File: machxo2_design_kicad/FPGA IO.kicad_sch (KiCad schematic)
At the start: 7 parts, among them J2 Conn_01x12_Pin, J3 Conn_01x12_Pin, Q3 DMG1012T, U3 LCMX02-256HC-4SG32C

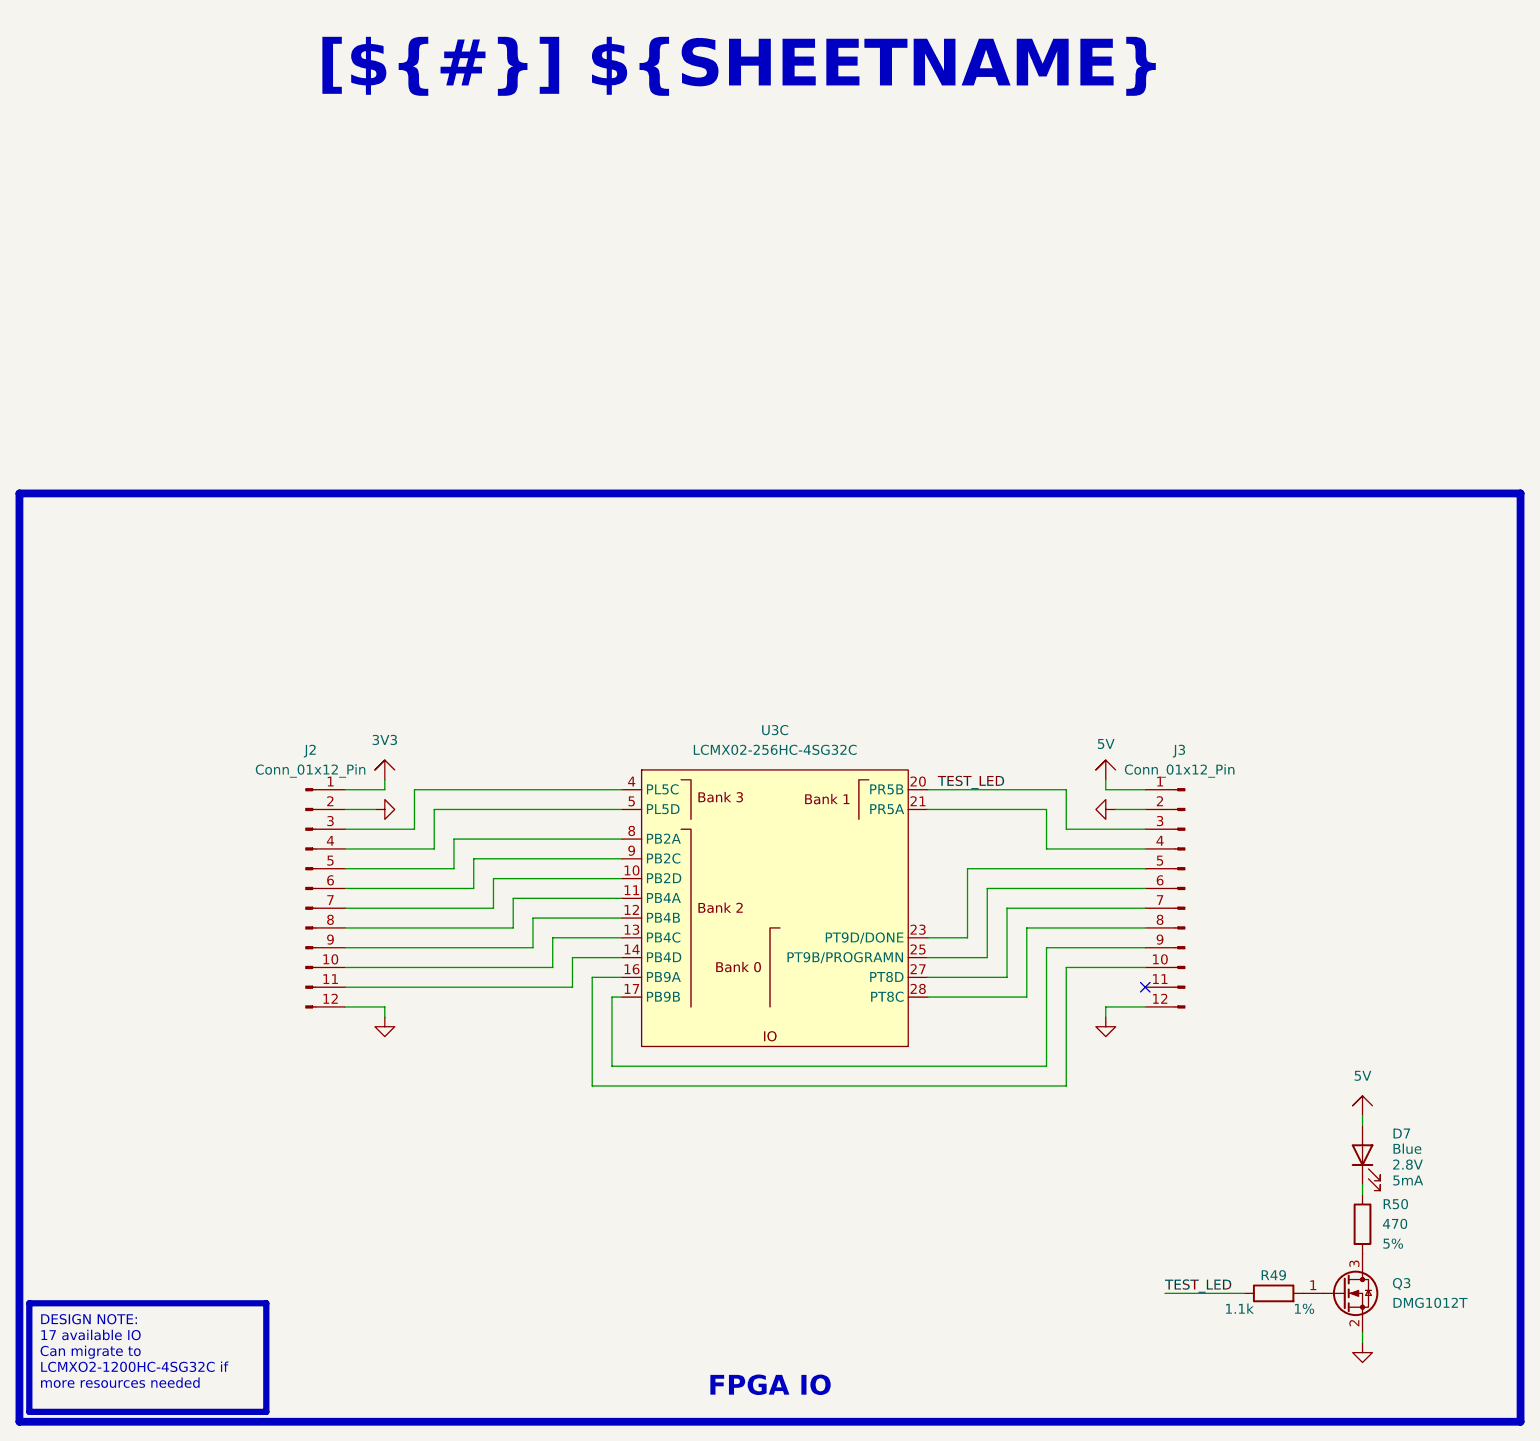
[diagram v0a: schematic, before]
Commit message: Schematic bom generated. Preliminary review down. Layout started.
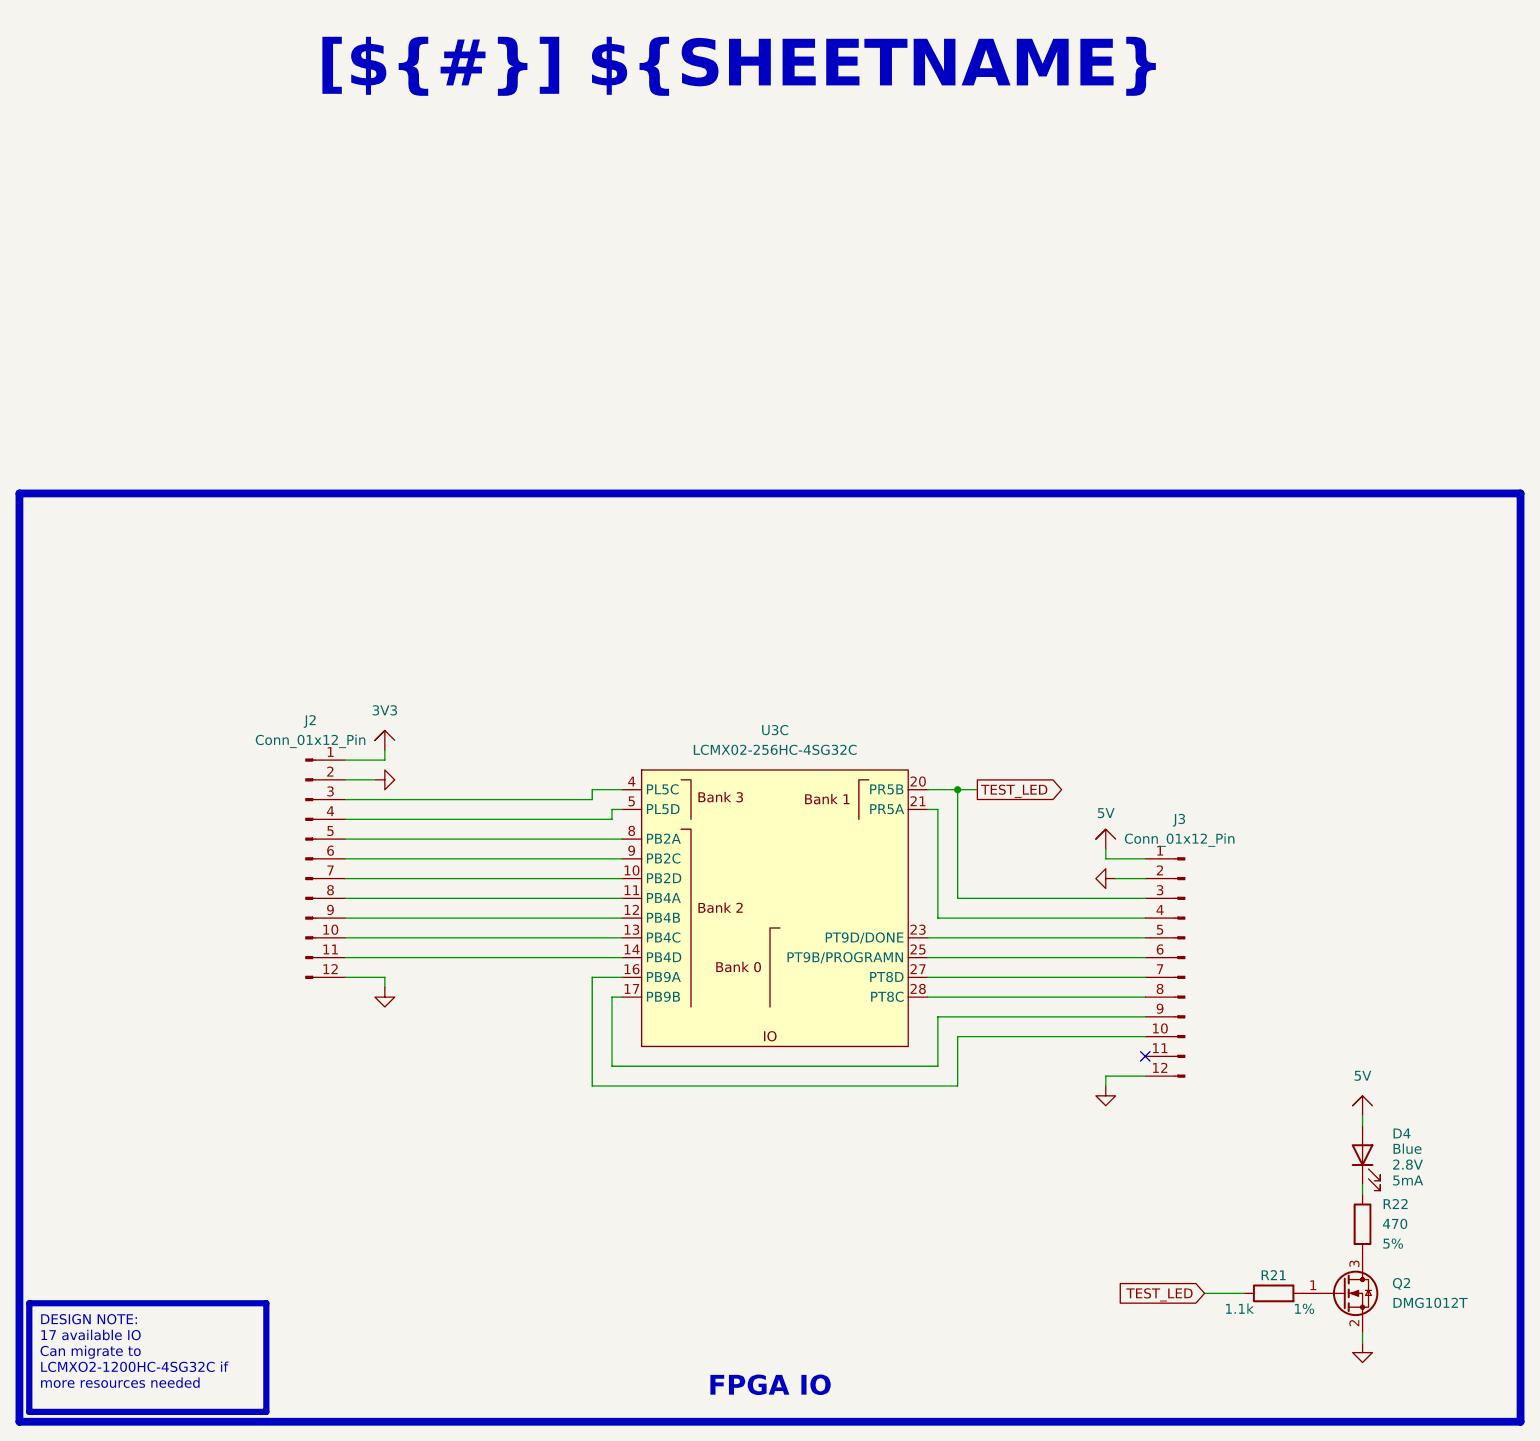
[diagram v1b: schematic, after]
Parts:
- J2, J3: footprint (none) -> Connector_PinHeader_2.54mm:PinHeader_1x12_P2.54mm_Vertical; Link (none) -> https://www.digikey.com/en/products/detail/molex/0022032121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; Part Number (none) -> 0022032121
- Q2: renamed from Q3; Link (none) -> https://www.digikey.com/en/products/detail/diodes-incorpora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; Part Number (none) -> DMG1012T-7
- R21: renamed from R49; footprint (none) -> Resistor_SMD:R_0402_1005Metric; Link (none) -> https://www.digikey.com/en/products/detail/yageo/RC0402FR-0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; Part Number (none) -> RC0402FR-071K1L
- R22: renamed from R50; footprint (none) -> Resistor_SMD:R_0402_1005Metric; Link (none) -> https://www.digikey.com/en/products/detail/yageo/RC0402FR-0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; Part Number (none) -> RC0402FR-07470RL
- U3: Link https://www.digikey.com/en/products/detail/lattice-semiconductor-corporation/LCMXO2-256HC-4SG32C/3232671?s=N4IgTCBcDaIDYGMC2APA9mAtGArANgAsFMAWAZwHMBmMBEAXQF8g -> https://www.digikey.com/en/products/detail/lattice-semiconductor-corporation/lcmxo2-256hc-4sg32c/3232671; Part Number (none) -> LCMXO2-256HC-4SG32C
- renumbered D7 to D4
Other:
- moved on the sheet: J2, J3
